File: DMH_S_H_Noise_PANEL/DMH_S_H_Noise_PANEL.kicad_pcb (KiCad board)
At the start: 2 copper layers, 50 x 200 mm, 5 parts, among them J0 Panel_GND_Solder_Wire_Pad

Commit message: Created front panel
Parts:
- added H10: Slw In, SynthStuff:Jack_6.35mm_Cutout_v3, F.Cu at (58.5, 190.2)
- added H11: S&H Out, SynthStuff:Jack_6.35mm_Cutout_Output_v6, F.Cu at (91.5, 171.8)
- added H12: Slw Out, SynthStuff:Jack_6.35mm_Cutout_Output_v6, F.Cu at (91.5, 190.2)
- added H13: White, SynthStuff:Jack_6.35mm_Cutout_Output_v6, F.Cu at (75.0, 208.8)
- added H14: Pink, SynthStuff:Jack_6.35mm_Cutout_Output_v6, F.Cu at (58.5, 208.8)
- added H15: Blue, SynthStuff:Jack_6.35mm_Cutout_Output_v6, F.Cu at (91.5, 208.8)
- added H5: Rate, SynthStuff:Pot_Cutout_Large_v2, F.Cu at (75.0, 66.0)
- added H6: CV Amount, SynthStuff:Pot_Cutout_Small, F.Cu at (75.0, 142.8)
- added H7: Slew, SynthStuff:Pot_Cutout_Small, F.Cu at (75.0, 107.0)
- added H8: CV In, SynthStuff:Jack_6.35mm_Cutout_v3, F.Cu at (58.5, 171.8)
- added H9: Clk In, SynthStuff:Jack_6.35mm_Cutout_v3, F.Cu at (75.0, 171.8)
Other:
- board text added: "S&H Noise"
- board text added: "mki"
- board text removed: "Module Name"
- board text removed: "TYPE"

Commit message: Completed circuit
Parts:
- H6: value CV Amount -> Input Level
- H8: value CV In -> Input

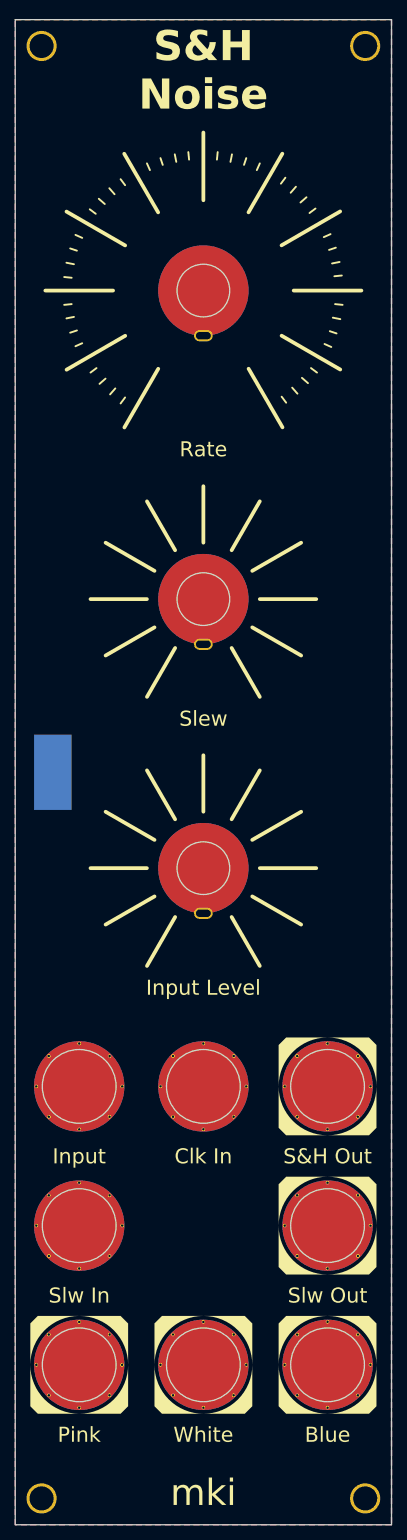
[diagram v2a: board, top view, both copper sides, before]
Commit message: Added Rate LED to the panel
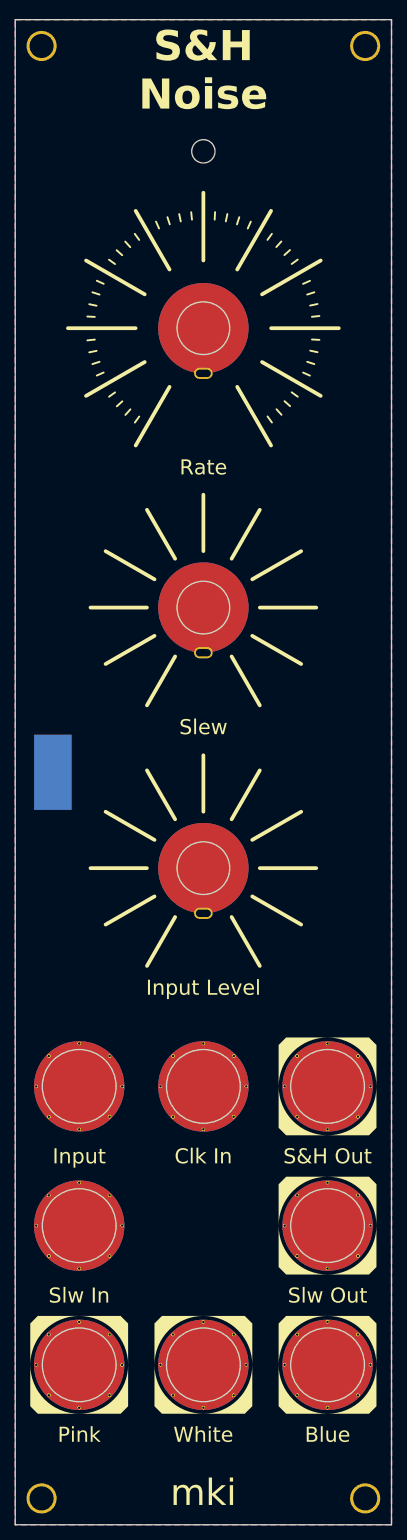
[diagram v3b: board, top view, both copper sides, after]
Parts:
- added H16: Rate LED, SynthStuff:MountingHole_LED_3mm, F.Cu at (75.0, 47.5)
- H5: footprint SynthStuff:Pot_Cutout_Large_v2 -> SynthStuff:Pot_Cutout_Medium_v2
- moved H5 5.00 mm to (75.0, 71.0)
- moved H7 1.12 mm to (75.0, 108.1)

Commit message: Manual trigger panel experiments ongoing
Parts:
- added H17: Switch, SynthStuff:MX_switch_Cutout, F.Cu at (75.0, 171.8)
- H10: value Slw In -> Slew In
- H11: value S&H Out -> S&H
- H12: value Slw Out -> Slew
- H9: value Clk In -> Clock
- moved H9 18.5 mm to (75.0, 190.2)
- moved H6 8.25 mm to (83.2, 142.8)
- moved H7 8.25 mm to (83.2, 108.1)

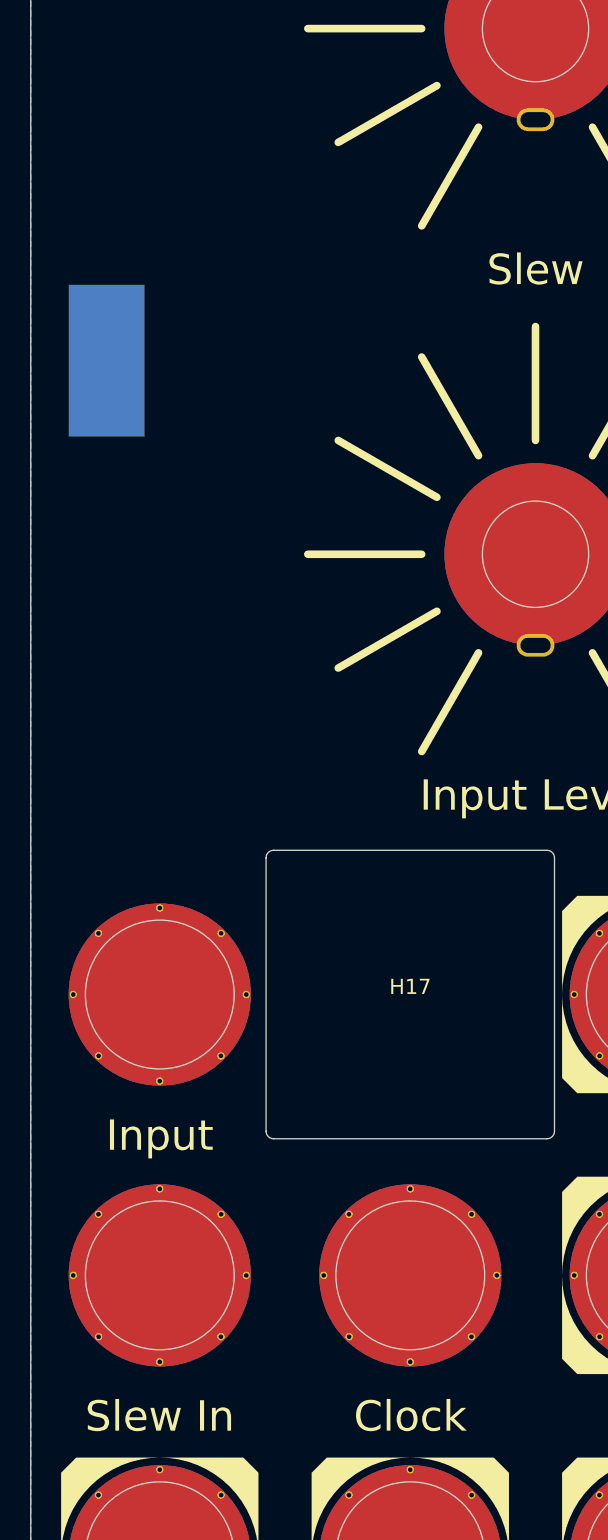
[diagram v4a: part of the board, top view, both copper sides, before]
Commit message: Added toggle switch for trigger source
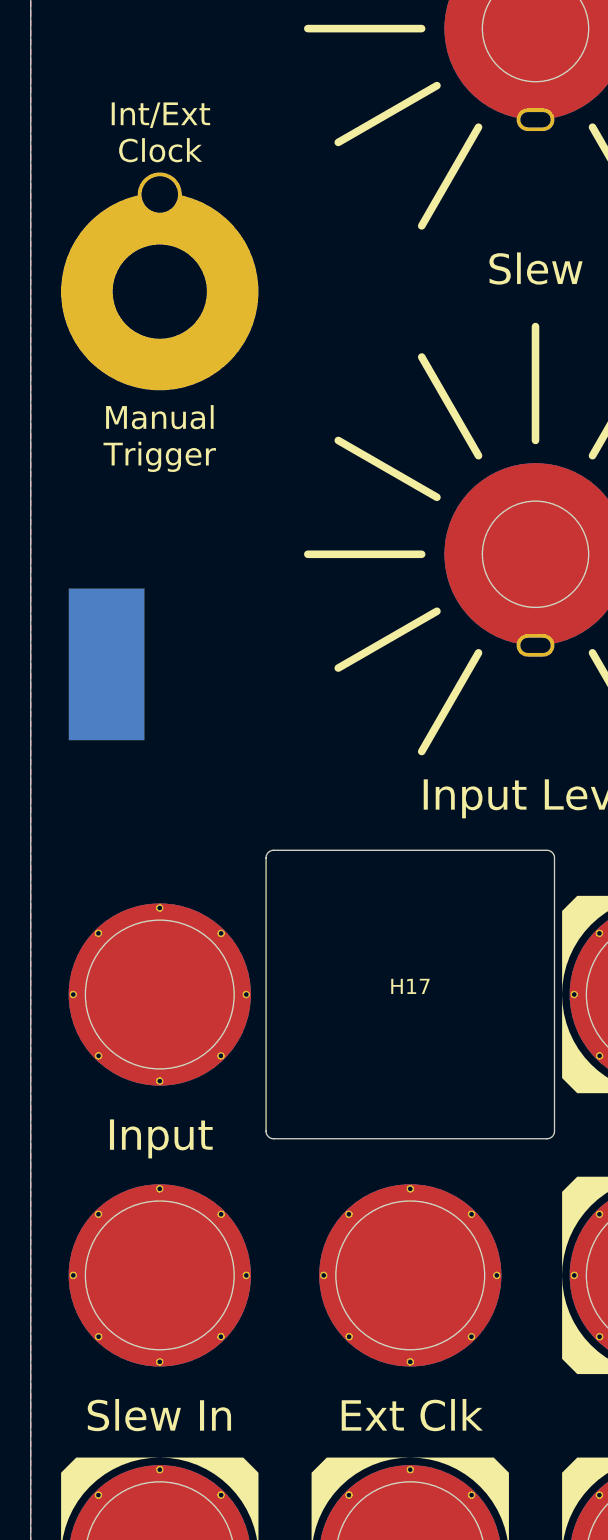
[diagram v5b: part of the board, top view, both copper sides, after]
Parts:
- added H18: Trigger Source, SynthStuff:Toggle_Switch_Cutout, F.Cu at (58.5, 125.5)
- H9: value Clock -> Ext Clk
- moved J0 20.0 mm to (55.0, 150.0)
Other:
- board text added: "Int/Ext Clock"
- board text added: "Manual Trigger"

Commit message: Finished front panel
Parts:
- H17: value Switch -> Manual Trigger
- H6, H7: footprint SynthStuff:Pot_Cutout_Small -> SynthStuff:Pot_Cutout_Tiny
- H9: value Ext Clk -> Ext.Clk
- moved H18 49.2 mm to (75.0, 171.8)
- moved H17 48.0 mm to (62.0, 125.5)
- moved H6 2.75 mm to (86.0, 142.8)
- moved H7 2.75 mm to (86.0, 108.1)
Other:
- board text added: "Clock"
- board text added: "Trigger"
- board text removed: "Int/Ext Clock"

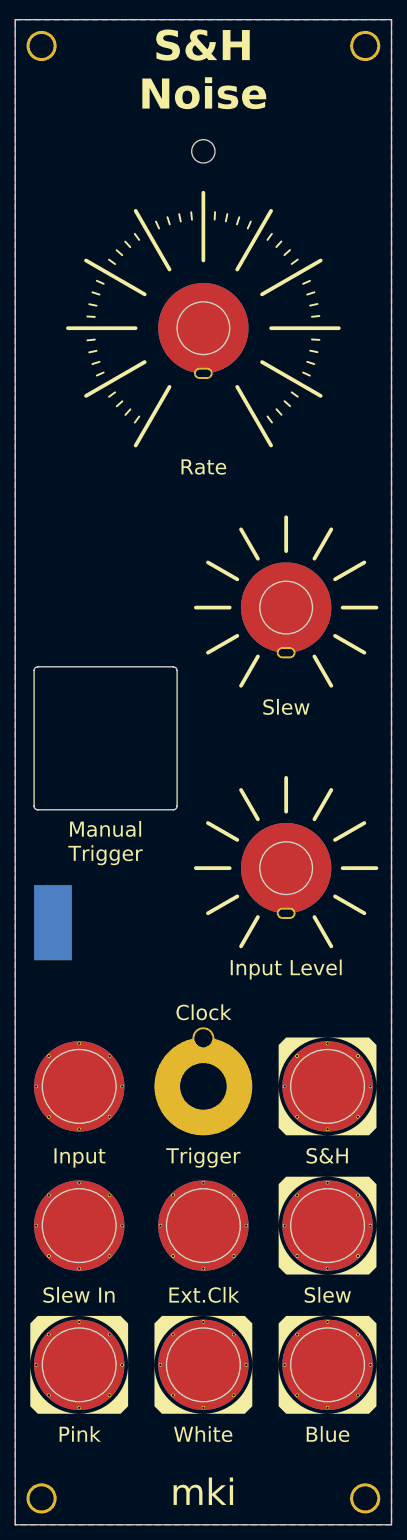
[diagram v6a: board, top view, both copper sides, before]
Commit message: Added clock output
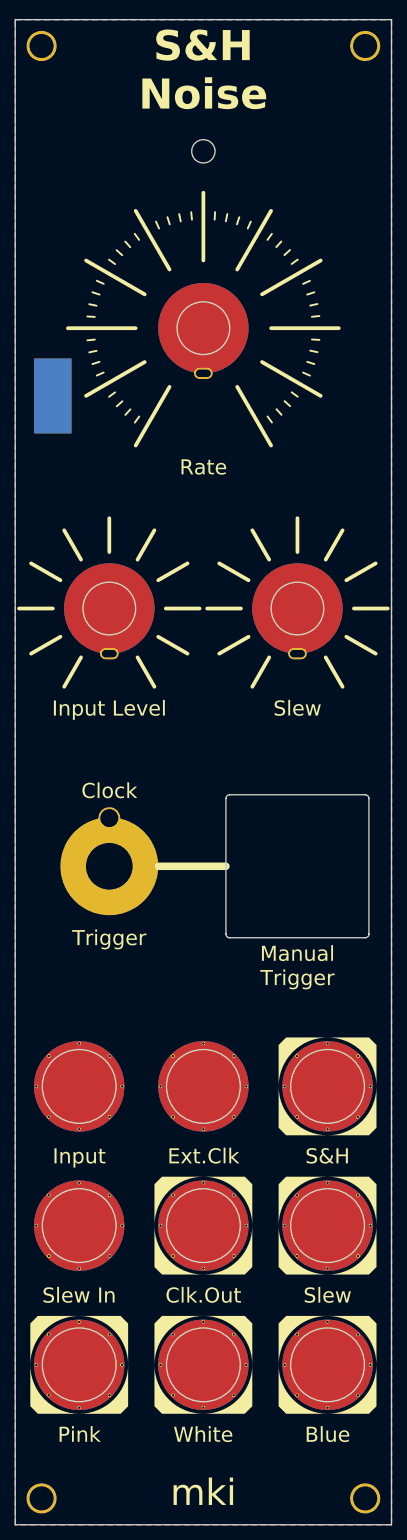
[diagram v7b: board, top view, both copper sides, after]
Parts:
- added H19: Clk.Out, SynthStuff:Jack_6.35mm_Cutout_Output_v6, F.Cu at (75.0, 190.2)
- moved J0 70.0 mm to (55.0, 80.0)
- moved H6 41.7 mm to (62.5, 108.2)
- moved H18 31.8 mm to (62.5, 142.5)
- moved H17 30.6 mm to (87.5, 142.5)
- moved H9 18.5 mm to (75.0, 171.8)
- moved H7 1.51 mm to (87.5, 108.2)
